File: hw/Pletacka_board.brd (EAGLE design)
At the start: 160 x 100 mm, 0 parts

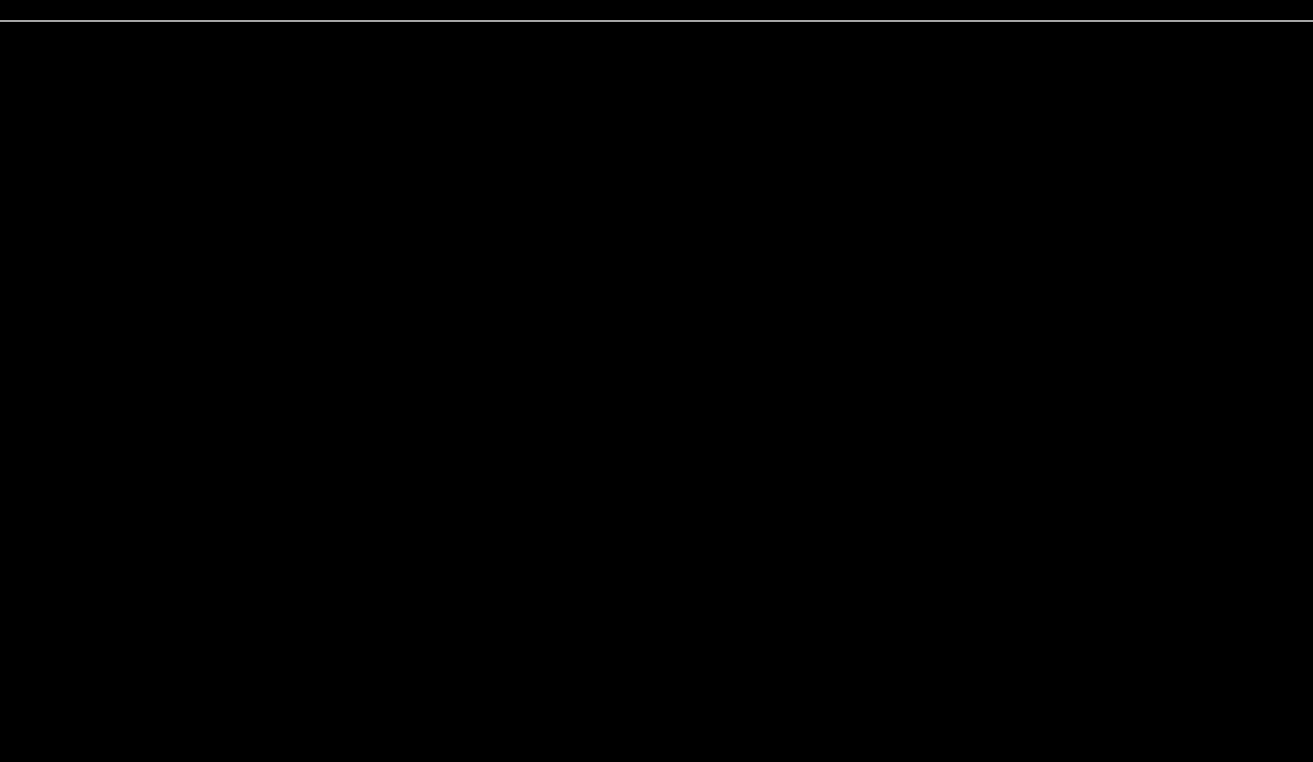
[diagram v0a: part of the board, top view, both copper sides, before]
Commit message: Add LEDs, RFID, Temp sen.
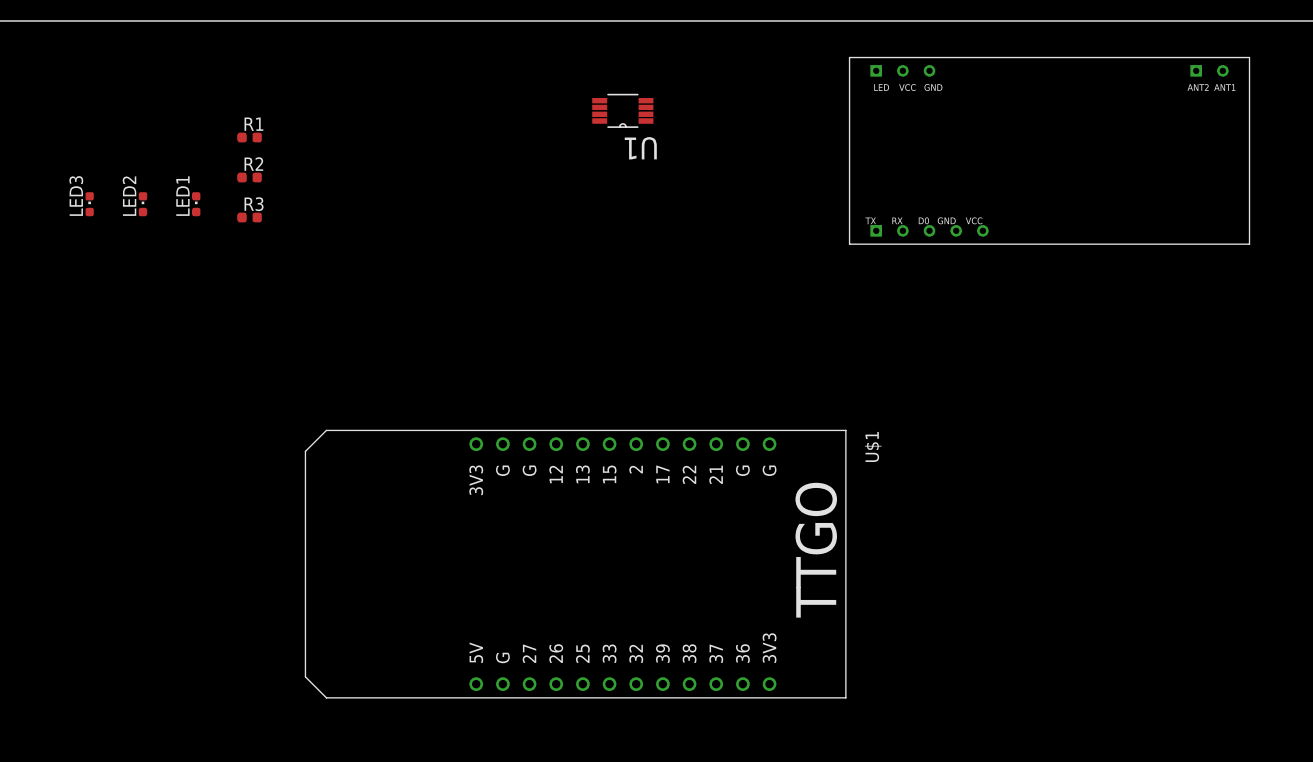
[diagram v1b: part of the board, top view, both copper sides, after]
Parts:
- added LED1, LED2, LED3: (no value), led:CHIPLED_0603
- added R1, R2, R3: (no value), rcl_upravena:R0603
- added RDM1: RDM6300, RDM6300:RDM6300
- added U$1: ESP-32-T-DISPLAY, ESP32-T-Display:ESP32-T-DISPLAY
- added U1: LM75BDP, LM75BDP:SOP65P490X110-8N
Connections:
- new net +3V3: U$1.3V3, U1.8
- new net +5V: RDM1.VCC, U$1.5V
- new net GND: LED1.C, LED2.C, LED3.C, RDM1.GND, U$1.G-1, U1.4
- new net LED_POWER: R1.1, U$1.25
- new net LED_SEND: R3.1, U$1.27
- new net LED_WIFI: R2.1, U$1.26
- new net N$1: LED1.A, R1.2
- new net N$11: U$1.33
- new net N$12: LED3.A, R3.2
- new net N$2: LED2.A, R2.2
- new net N$3: U$1.17
- new net N$4: U$1.2
- new net N$5: U$1.15
- new net N$6: U$1.13
- new net N$7: U$1.12
- new net OPTO1: U$1.36
- new net OPTO2: U$1.37
- new net OPTO3: U$1.38
- new net OPTO4: U$1.39
- new net RFID: RDM1.RX, U$1.32
- new net TMP_SCL: U$1.22, U1.2
- new net TMP_SDA: U$1.21, U1.1
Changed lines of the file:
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@@
 </autorouter>
 <elements>
+<element name="U$1" library="ESP32-T-Display" package="ESP32-T-DISPLAY" value="ESP-32-T-DISPLAY" x="69.85" y="48.26" smashed="yes" rot="R270">
+<attribute name="NAME" x="108.199665625" y="60.998" size="1.27" layer="25" rot="R270"/>
+<attribute name="VALUE" x="108.335334375" y="42.583" size="1.27" layer="27" rot="R270"/>
+</element>
+<element name="RDM1" library="RDM6300" package="RDM6300" value="RDM6300" x="125.73" y="87.63" smashed="yes" rot="R180">
+<attribute name="AVAILABILITY" value="Unavailable" x="125.73" y="87.63" size="1.778" layer="27" rot="R180" display="off"/>
+<attribute name="DESCRIPTION" value=" RDM6300 125KHz cardreader mini-module is designed for reading code from 125KHz card compatible read-only tags and read/write card. " x="125.73" y="87.63" size="1.778" layer="27" rot="R180" display="off"/>
+<attribute name="MF" value="ITEAD" x="125.73" y="87.63" size="1.778" layer="27" rot="R180" display="off"/>
+<attribute name="MP" value="RDM6300" x="125.73" y="87.63" size="1.778" layer="27" rot="R180" display="off"/>
+<attribute name="PACKAGE" value="Package " x="125.73" y="87.63" size="1.778" layer="27" rot="R180" display="off"/>
+<attribute name="PRICE" value="None" x="125.73" y="87.63" size="1.778" layer="27" rot="R180" display="off"/>
+</element>
+<element name="U1" library="LM75BDP" package="SOP65P490X110-8N" value="LM75BDP" x="85.09" y="91.44" smashed="yes" rot="R180">
+<attribute name="AVAILABILITY" value="Unavailable" x="85.09" y="91.44" size="1.778" layer="27" rot="R180" display="off"/>
+<attribute name="DESCRIPTION" value=" Temperature Sensor Digital, Local -55°C ~ 125°C 11 b 8-TSSOP " x="85.09" y="91.44" size="1.778" layer="27" rot="R180" display="off"/>
+<attribute name="MF" value="NXP Semiconductors" x="85.09" y="91.44" size="1.778" layer="27" rot="R180" display="off"/>
+<attribute name="MP" value="LM75BDP" x="85.09" y="91.44" size="1.778" layer="27" rot="R180" display="off"/>
+<attribute name="NAME" x="88.545" y="88.899559375" size="2.083159375" layer="25" ratio="10" rot="SR180"/>
+<attribute name="PACKAGE" value="TSSOP-8 NXP Semiconductors" x="85.09" y="91.44" size="1.778" layer="27" rot="R180" display="off"/>
+<attribute name="PRICE" value="None" x="85.09" y="91.44" size="1.778" layer="27" rot="R180" display="off"/>
+<attribute name="VALUE" x="88.54816875" y="95.88985" size="2.08506875" layer="27" ratio="10" rot="SR180"/>
+</element>
+<element name="R1" library="rcl_upravena" package="R0603" value="" x="49.53" y="88.9" smashed="yes">
+<attribute name="NAME" x="48.895" y="89.535" size="1.27" layer="25"/>
+<attribute name="VALUE" x="48.895" y="86.995" size="1.27" layer="27"/>
+</element>
+<element name="R2" library="rcl_upravena" package="R0603" value="" x="49.53" y="85.09" smashed="yes">
+<attribute name="NAME" x="48.895" y="85.725" size="1.27" layer="25"/>
+<attribute name="VALUE" x="48.895" y="83.185" size="1.27" layer="27"/>
+</element>
+<element name="R3" library="rcl_upravena" package="R0603" value="" x="49.53" y="81.28" smashed="yes">
+<attribute name="NAME" x="48.895" y="81.915" size="1.27" layer="25"/>
+<attribute name="VALUE" x="48.895" y="79.375" size="1.27" layer="27"/>
+</element>
+<element name="LED1" library="led" package="CHIPLED_0603" package3d_urn="urn:adsk.eagle:package:15822/2" value="" x="44.45" y="82.55" smashed="yes">
+<attribute name="NAME" x="43.815" y="81.28" size="1.27" layer="25" rot="R90"/>
+<attribute name="POPULARITY" value="28" x="44.45" y="82.55" size="1.778" layer="27" display="off"/>
+<attribute name="VALUE" x="46.355" y="81.28" size="1.27" layer="27" rot="R90"/>
+</element>
+<element name="LED2" library="led" package="CHIPLED_0603" package3d_urn="urn:adsk.eagle:package:15822/2" value="" x="39.37" y="82.55" smashed="yes">
+<attribute name="NAME" x="38.735" y="81.28" size="1.27" layer="25" rot="R90"/>
+<attribute name="POPULARITY" value="28" x="39.37" y="82.55" size="1.778" layer="27" display="off"/>
+<attribute name="VALUE" x="41.275" y="81.28" size="1.27" layer="27" rot="R90"/>
+</element>
+<element name="LED3" library="led" package="CHIPLED_0603" package3d_urn="urn:adsk.eagle:package:15822/2" value="" x="34.29" y="82.55" smashed="yes">
+<attribute name="NAME" x="33.655" y="81.28" size="1.27" layer="25" rot="R90"/>
+<attribute name="POPULARITY" value="28" x="34.29" y="82.55" size="1.778" layer="27" display="off"/>
+<attribute name="VALUE" x="36.195" y="81.28" size="1.27" layer="27" rot="R90"/>
+</element>
 </elements>
 <signals>
+<signal name="GND">
+<contactref element="U$1" pad="G-1"/>
+<contactref element="RDM1" pad="GND"/>
+<contactref element="U1" pad="4"/>
+<contactref element="LED1" pad="C"/>
+<contactref element="LED2" pad="C"/>
+<contactref element="LED3" pad="C"/>
+<wire x1="99.06" y1="59.69" x2="116.84" y2="80.01" width="0" layer="19" extent="1-1"/>
+<wire x1="87.2998" y1="92.4052" x2="116.84" y2="80.01" width="0" layer="19" extent="1-1"/>
+<wire x1="44.45" y1="83.3" x2="99.06" y2="59.69" width="0" layer="19" extent="1-1"/>
+<wire x1="39.37" y1="83.3" x2="44.45" y2="83.3" width="0" layer="19" extent="1-1"/>
+<wire x1="34.29" y1="83.3" x2="39.37" y2="83.3" width="0" layer="19" extent="1-1"/>
+</signal>
+<signal name="+3V3">
+<contactref element="U$1" pad="3V3"/>
+<contactref element="U1" pad="8"/>
+<wire x1="82.8802" y1="90.4748" x2="71.12" y2="59.69" width="0" layer="19" extent="1-1"/>
+</signal>
+<signal name="+5V">
+<contactref element="U$1" pad="5V"/>
+<contactref element="RDM1" pad="VCC"/>
+<wire x1="119.38" y1="80.01" x2="71.12" y2="36.83" width="0" layer="19" extent="1-1"/>
+</signal>
+<signal name="TMP_SDA">
+<contactref element="U$1" pad="21"/>
+<contactref element="U1" pad="1"/>
+<wire x1="87.2998" y1="90.4748" x2="93.98" y2="59.69" width="0" layer="19" extent="1-1"/>
+</signal>
+<signal name="TMP_SCL">
+<contactref element="U$1" pad="22"/>
+<contactref element="U1" pad="2"/>
+<wire x1="87.2998" y1="91.1098" x2="91.44" y2="59.69" width="0" layer="19" extent="1-1"/>
+</signal>
+<signal name="N$3">
+<contactref element="U$1" pad="17"/>
+</signal>
+<signal name="N$4">
+<contactref element="U$1" pad="2"/>
+</signal>
+<signal name="N$5">
+<contactref element="U$1" pad="15"/>
+</signal>
+<signal name="N$6">
+<contactref element="U$1" pad="13"/>
+</signal>
+<signal name="N$7">
+<contactref element="U$1" pad="12"/>
+</signal>
+<signal name="N$11">
+<contactref element="U$1" pad="33"/>
+</signal>
+<signal name="RFID">
+<contactref element="U$1" pad="32"/>
+<contactref element="RDM1" pad="RX"/>
+<wire x1="111.76" y1="80.01" x2="86.36" y2="36.83" width="0" layer="19" extent="1-1"/>
+</signal>
+<signal name="OPTO4">
+<contactref element="U$1" pad="39"/>
+</signal>
+<signal name="OPTO3">
+<contactref element="U$1" pad="38"/>
+</signal>
+<signal name="OPTO2">
+<contactref element="U$1" pad="37"/>
+</signal>
+<signal name="OPTO1">
+<contactref element="U$1" pad="36"/>
+</signal>
+<signal name="N$1">
+<contactref element="R1" pad="2"/>
+<contactref element="LED1" pad="A"/>
+<wire x1="50.25" y1="88.9" x2="44.45" y2="81.8" width="0" layer="19" extent="1-1"/>
+</signal>
+<signal name="N$2">
+<contactref element="R2" pad="2"/>
+<contactref element="LED2" pad="A"/>
+<wire x1="50.25" y1="85.09" x2="39.37" y2="81.8" width="0" layer="19" extent="1-1"/>
+</signal>
+<signal name="N$12">
+<contactref element="R3" pad="2"/>
+<contactref element="LED3" pad="A"/>
+<wire x1="50.25" y1="81.28" x2="34.29" y2="81.8" width="0" layer="19" extent="1-1"/>
+</signal>
+<signal name="LED_POWER">
+<contactref element="R1" pad="1"/>
+<contactref element="U$1" pad="25"/>
+<wire x1="81.28" y1="36.83" x2="48.81" y2="88.9" width="0" layer="19" extent="1-1"/>
+</signal>
+<signal name="LED_WIFI">
+<contactref element="R2" pad="1"/>
+<contactref element="U$1" pad="26"/>
+<wire x1="78.74" y1="36.83" x2="48.81" y2="85.09" width="0" layer="19" extent="1-1"/>
+</signal>
+<signal name="LED_SEND">
+<contactref element="R3" pad="1"/>
+<contactref element="U$1" pad="27"/>
+<wire x1="76.2" y1="36.83" x2="48.81" y2="81.28" width="0" layer="19" extent="1-1"/>
+</signal>
 </signals>
 <mfgpreviewcolors>
@@
 </board>
 </drawing>
+<compatibility>
+<note version="8.3" severity="warning">
+Since Version 8.3, EAGLE supports URNs for individual library
+assets (packages, symbols, and devices). The URNs of those assets
+will not be understood (or retained) with this version.
+</note>
+<note version="8.3" severity="warning">
+Since Version 8.3, EAGLE supports the association of 3D packages
+with devices in libraries, schematics, and board files. Those 3D
+packages will not be understood (or retained) with this version.
+</note>
+</compatibility>
 </eagle>

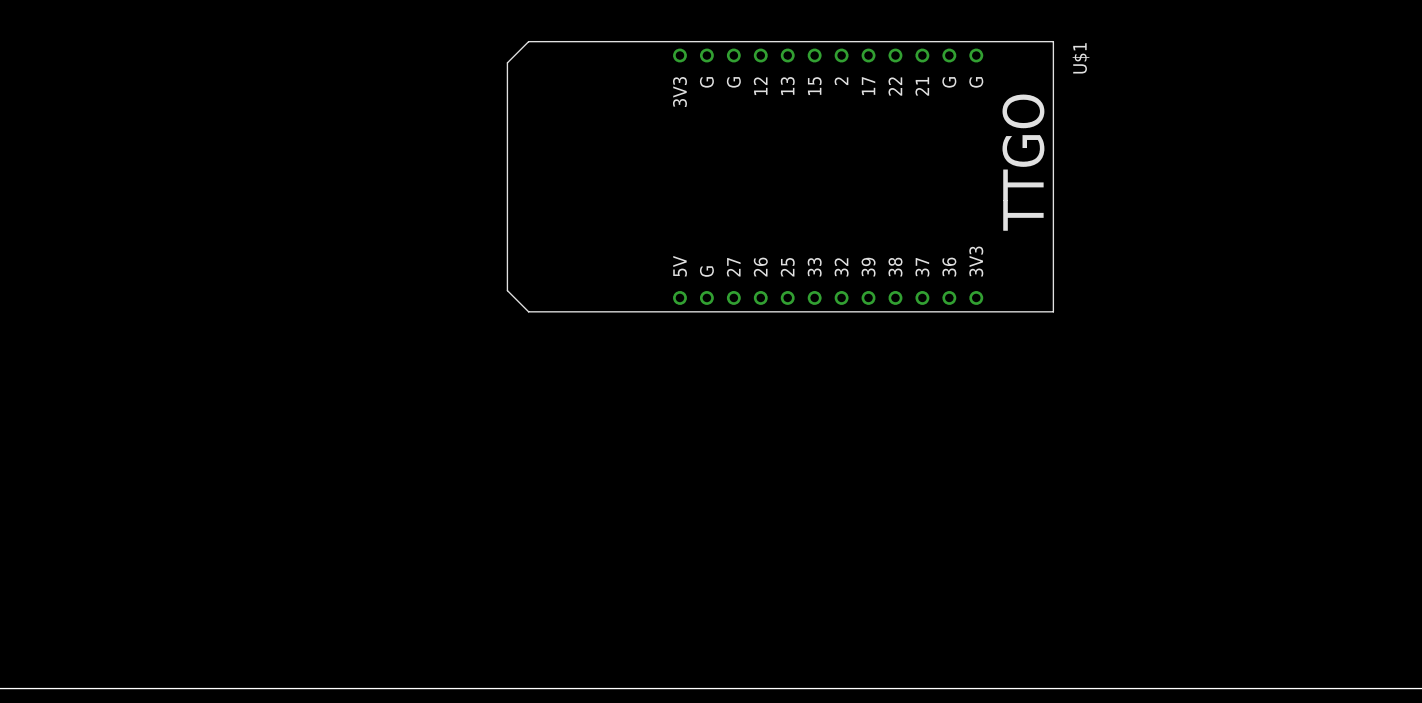
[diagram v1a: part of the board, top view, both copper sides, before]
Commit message: Add Buttons + optocouplers
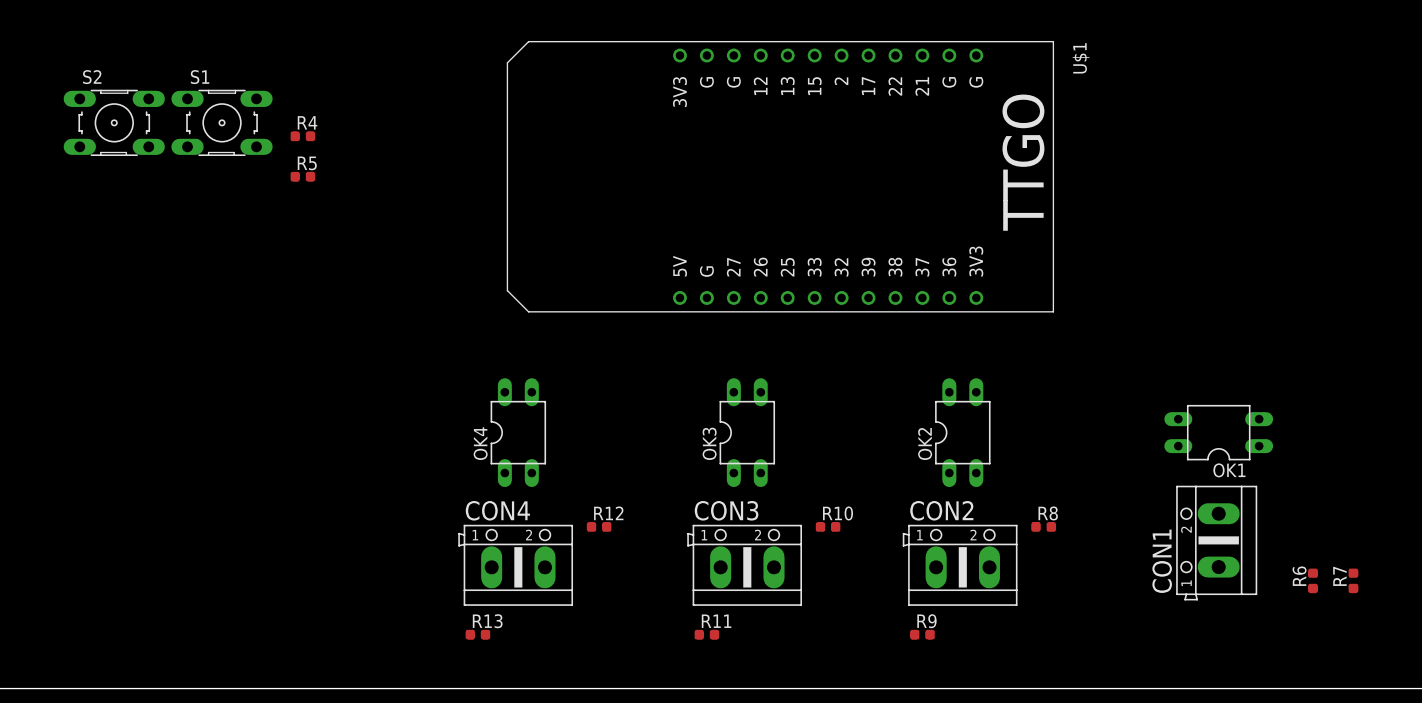
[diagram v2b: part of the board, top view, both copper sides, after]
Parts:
- added CON1, CON2, CON3, CON4: (no value), #Svorkovnice:AK500/2
- added OK1, OK2, OK3, OK4: PC817, #Optocleny:DIL04
- added R10, R11, R12, R13, R6, R7, R8, R9: (no value), rcl_upravena:R0603
- added R4, R5: 330R, rcl_upravena:R0603
- added S1, S2: (no value), switch-omron:B3F-10XX
- R1, R2, R3: value (none) -> 330R
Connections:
- new net BUTTON1: R4.1, U$1.13
- new net BUTTON2: R5.1, U$1.12
- new net N$10: R5.2, S2.3, S2.4
- new net N$13: CON2.1, R8.1
- new net N$14: CON2.2, OK2.2
- new net N$15: OK2.1, R8.2
- new net N$16: CON3.1, R10.1
- new net N$17: CON3.2, OK3.2
- new net N$18: OK3.1, R10.2
- new net N$19: CON4.1, R12.1
- new net N$20: CON4.2, OK4.2
- new net N$21: OK4.1, R12.2
- new net N$8: R4.2, S1.3, S1.4
- new net N$9: OK1.1, R6.2
- net +3V3: now also R11.2, R13.2, R7.2, R9.2
- net GND: now also OK1.3, OK2.3, OK3.3, OK4.3, S1.1, S1.2, S2.1, S2.2
- net N$6: now also CON1.1, R6.1; no longer U$1.13
- net N$7: now also CON1.2, OK1.2; no longer U$1.12
- net OPTO1: now also OK1.4, R7.1
- net OPTO2: now also OK2.4, R9.1
- net OPTO3: now also OK3.4, R11.1
- net OPTO4: now also OK4.4, R13.1
